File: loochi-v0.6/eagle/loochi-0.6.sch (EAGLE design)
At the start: 51 parts, among them IC1 ATTINY61M, J1 SPI_PRG, J2 POWER_JACKSMT3, P1 53047-0610, Q1 PMN25ENSOT457, Q2 PMN25ENSOT457, Q3 PMN25ENSOT457, U1 BLE112, U2 LZ4-00MC00BIGPADS, U3 LP2985

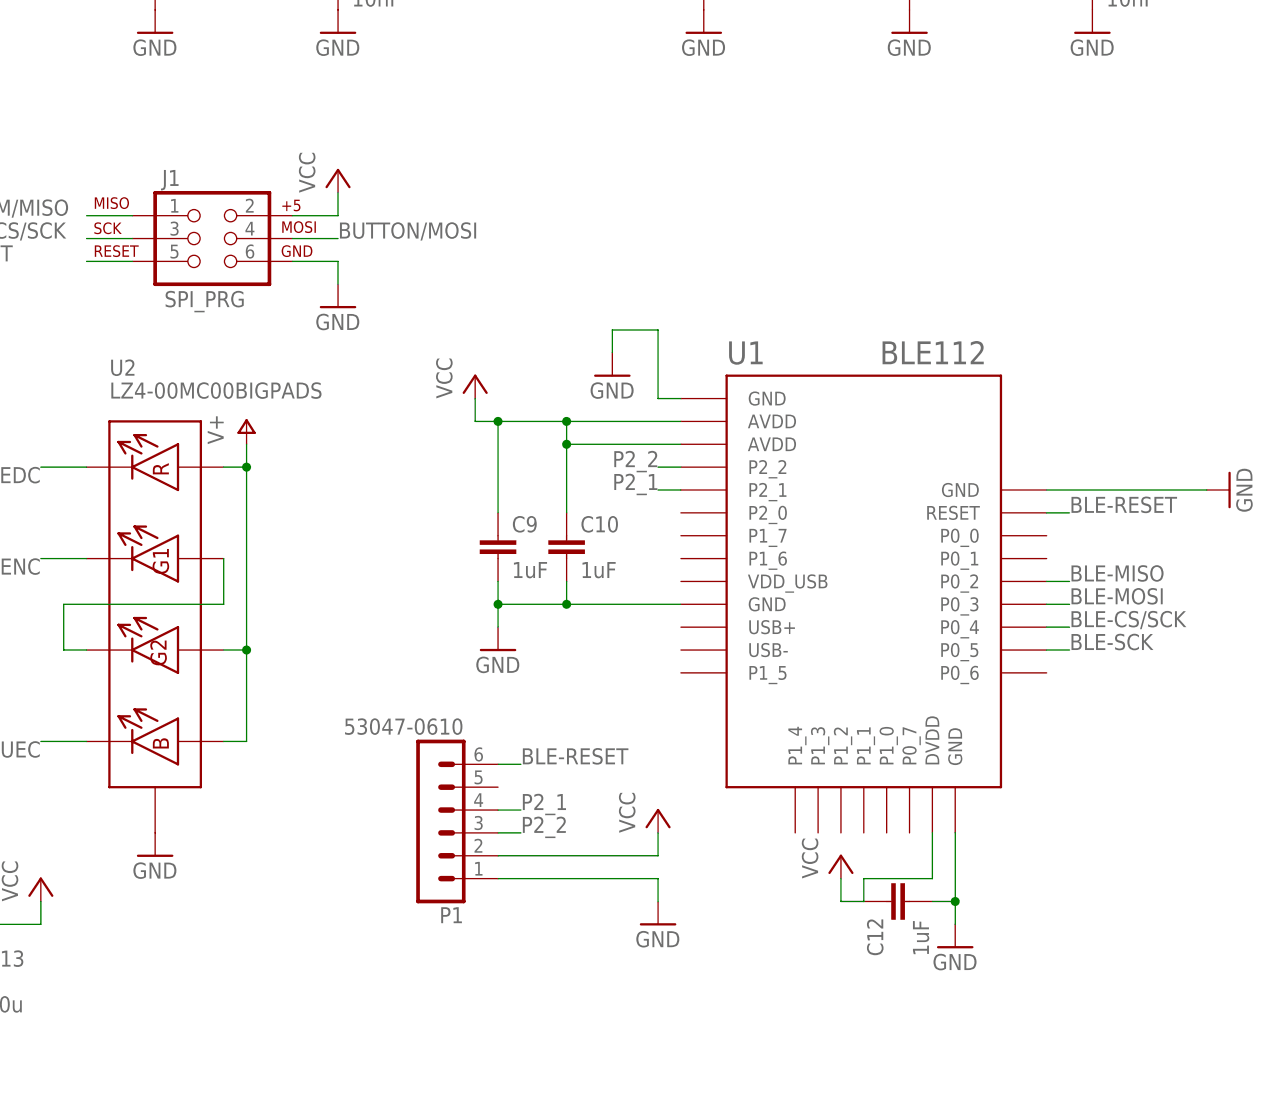
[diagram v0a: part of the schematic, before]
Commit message: Routed connections + Added SPI on BLE connector + Some cleaning/Rework
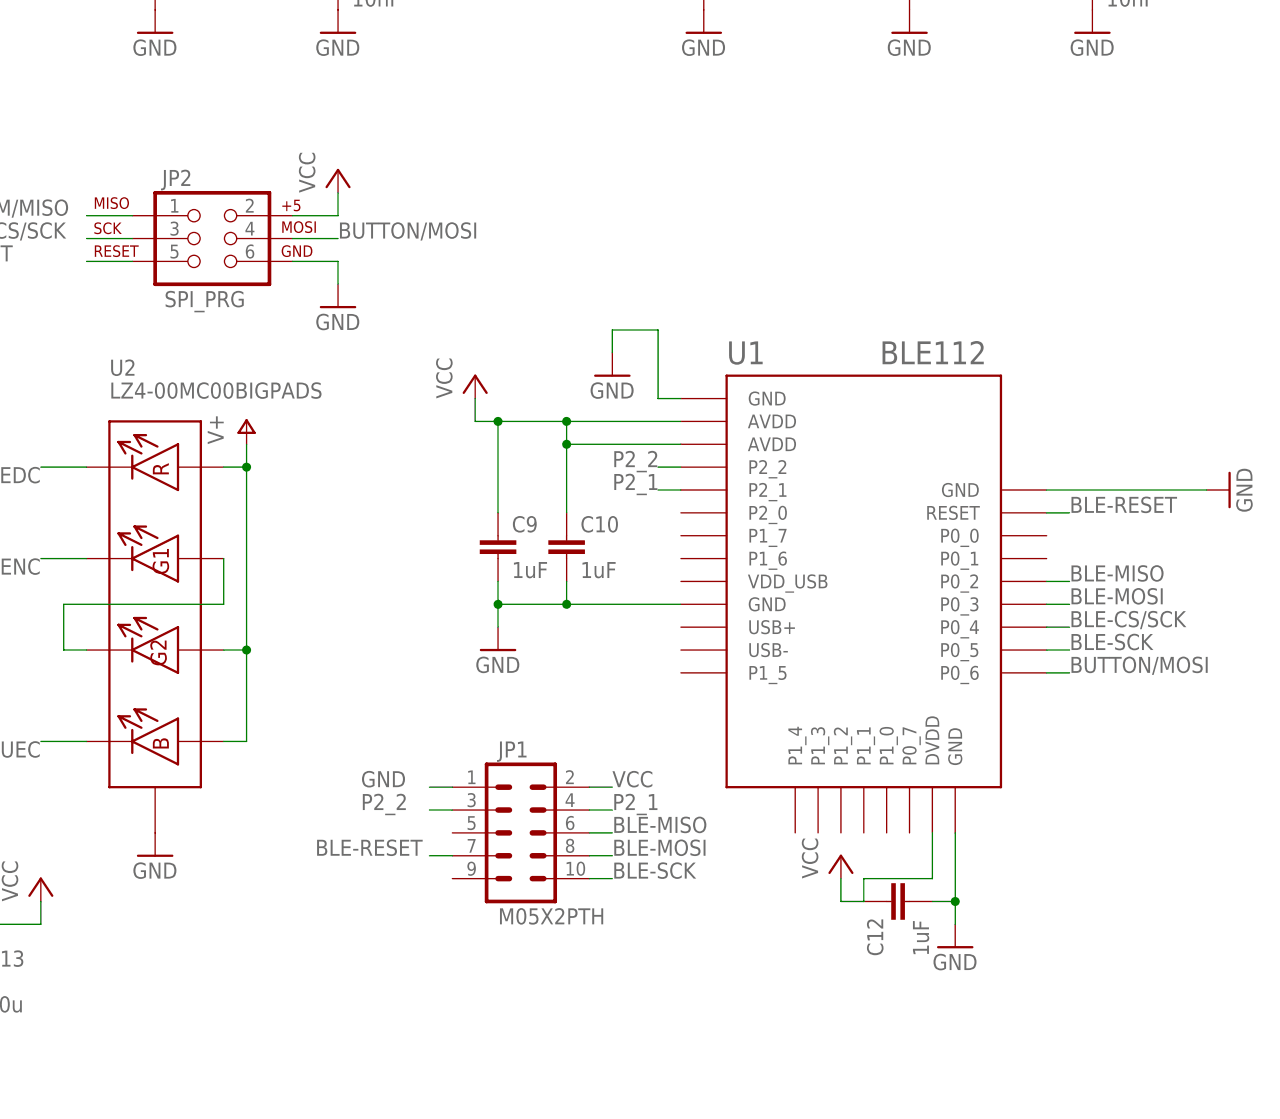
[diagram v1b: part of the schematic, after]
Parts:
- removed P1: 53047-0610, con-molex-picoblade:53047-0610
- added JP1: M05X2PTH, SparkFun:M05X2PTH
- renumbered J1 to JP2
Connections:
- net BLE-MISO: now also JP1.6
- net BLE-MOSI: now also JP1.8
- net BLE-RESET: now also JP1.7; no longer P1.6
- net BLE-SCK: now also JP1.10
- net BUTTON/MOSI: now also U1.P0_6
- net GND: now also JP1.1; no longer P1.1
- net P2_1: now also JP1.4; no longer P1.4
- net P2_2: now also JP1.3; no longer P1.3
- net VCC: now also JP1.2; no longer P1.2
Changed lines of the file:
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@@
 <parts>
 <part name="J2" library="power-connectors" deviceset="POWER_JACK" device="SMT3"/>
-<part name="J1" library="SparkFun" deviceset="AVR_SPI_PRG_6" device="NS" value="SPI_PRG"/>
+<part name="JP2" library="SparkFun" deviceset="AVR_SPI_PRG_6" device="NS" value="SPI_PRG"/>
 <part name="C7" library="rcl" deviceset="C-EU" device="C0603" value="0.1uF"/>
 <part name="C8" library="rcl" deviceset="C-EU" device="C0603" value="0.1uF"/>
@@
 <part name="C12" library="rcl" deviceset="C-EU" device="C0603" value="1uF"/>
 <part name="GND20" library="supply1" deviceset="GND" device=""/>
-<part name="P1" library="con-molex-picoblade" deviceset="53047-0610" device="">
-<attribute name="PARTNO" value="*"/>
-</part>
-<part name="P+10" library="supply1" deviceset="VCC" device=""/>
-<part name="GND21" library="supply1" deviceset="GND" device=""/>
 <part name="P+11" library="supply1" deviceset="VCC" device=""/>
 <part name="D4" library="diode-schottky" deviceset="DIODE-SCHOTTKY" device="D0603"/>
 <part name="D5" library="diode-schottky" deviceset="DIODE-SCHOTTKY" device="" value="PMEG4010CEH"/>
 <part name="S1" library="buttons" deviceset="TAC_SWITCH" device=""/>
+<part name="JP1" library="SparkFun" deviceset="M05X2" device="PTH"/>
 </parts>
 <sheets>
@@
 <instances>
 <instance part="J2" gate="G$1" x="15.24" y="20.32"/>
-<instance part="J1" gate="G$1" x="137.16" y="106.68"/>
+<instance part="JP2" gate="G$1" x="137.16" y="106.68"/>
 <instance part="C7" gate="G$1" x="12.7" y="101.6" smashed="yes" rot="R90">
 <attribute name="NAME" x="12.319" y="103.124" size="1.778" layer="95" rot="R90"/>
@@
 </instance>
 <instance part="GND20" gate="1" x="220.98" y="27.94"/>
-<instance part="P1" gate="G$1" x="165.1" y="43.18" rot="R180">
-<attribute name="PARTNO" x="165.1" y="43.18" size="1.778" layer="96" rot="R270" display="off"/>
-</instance>
-<instance part="P+10" gate="VCC" x="187.96" y="43.18"/>
-<instance part="GND21" gate="1" x="187.96" y="30.48"/>
 <instance part="P+11" gate="VCC" x="208.28" y="38.1"/>
 <instance part="D4" gate="G$1" x="93.98" y="40.64" rot="R180"/>
@@
 </instance>
 <instance part="S1" gate="S" x="40.64" y="53.34"/>
+<instance part="JP1" gate="G$1" x="172.72" y="40.64"/>
 </instances>
 <busses>
@@
 <net name="BUTTON/MOSI" class="0">
 <segment>
-<pinref part="J1" gate="G$1" pin="4"/>
+<pinref part="JP2" gate="G$1" pin="4"/>
 <wire x1="147.32" y1="106.68" x2="152.4" y2="106.68" width="0.1524" layer="91"/>
 <label x="152.4" y="106.68" size="1.778" layer="95"/>
@@
 <wire x1="45.72" y1="53.34" x2="50.8" y2="53.34" width="0.1524" layer="91"/>
 </segment>
+<segment>
+<pinref part="U1" gate="G$1" pin="P0_6"/>
+<wire x1="231.14" y1="58.42" x2="233.68" y2="58.42" width="0.1524" layer="91"/>
+<label x="233.68" y="58.42" size="1.778" layer="95"/>
+</segment>
 </net>
 <net name="RESET" class="0">
 <segment>
-<pinref part="J1" gate="G$1" pin="5"/>
+<pinref part="JP2" gate="G$1" pin="5"/>
 <wire x1="129.54" y1="104.14" x2="124.46" y2="104.14" width="0.1524" layer="91"/>
 <label x="109.22" y="104.14" size="1.778" layer="95"/>
@@
 <net name="BLE-CS/SCK" class="0">
 <segment>
-<pinref part="J1" gate="G$1" pin="3"/>
+<pinref part="JP2" gate="G$1" pin="3"/>
 <wire x1="129.54" y1="106.68" x2="124.46" y2="106.68" width="0.1524" layer="91"/>
 <label x="109.22" y="106.68" size="1.778" layer="95"/>
@@
 </segment>
 <segment>
-<pinref part="J1" gate="G$1" pin="6"/>
+<pinref part="JP2" gate="G$1" pin="6"/>
 <wire x1="147.32" y1="104.14" x2="152.4" y2="104.14" width="0.1524" layer="91"/>
 <wire x1="152.4" y1="104.14" x2="152.4" y2="101.6" width="0.1524" layer="91"/>
@@
 </segment>
 <segment>
-<pinref part="P1" gate="G$1" pin="1"/>
-<wire x1="170.18" y1="35.56" x2="187.96" y2="35.56" width="0.1524" layer="91"/>
-<wire x1="187.96" y1="35.56" x2="187.96" y2="33.02" width="0.1524" layer="91"/>
-<pinref part="GND21" gate="1" pin="GND"/>
+<pinref part="JP1" gate="G$1" pin="1"/>
+<wire x1="165.1" y1="45.72" x2="162.56" y2="45.72" width="0.1524" layer="91"/>
+<label x="154.94" y="45.72" size="1.778" layer="95"/>
 </segment>
 </net>
@@
 </segment>
 <segment>
-<pinref part="J1" gate="G$1" pin="2"/>
+<pinref part="JP2" gate="G$1" pin="2"/>
 <wire x1="147.32" y1="109.22" x2="152.4" y2="109.22" width="0.1524" layer="91"/>
 <wire x1="152.4" y1="109.22" x2="152.4" y2="111.76" width="0.1524" layer="91"/>
@@
 </segment>
 <segment>
-<pinref part="P1" gate="G$1" pin="2"/>
-<wire x1="170.18" y1="38.1" x2="187.96" y2="38.1" width="0.1524" layer="91"/>
-<wire x1="187.96" y1="38.1" x2="187.96" y2="40.64" width="0.1524" layer="91"/>
-<pinref part="P+10" gate="VCC" pin="VCC"/>
-</segment>
-<segment>
 <pinref part="P+11" gate="VCC" pin="VCC"/>
 <wire x1="208.28" y1="35.56" x2="208.28" y2="33.02" width="0.1524" layer="91"/>
@@
 <wire x1="218.44" y1="35.56" x2="218.44" y2="40.64" width="0.1524" layer="91"/>
 </segment>
+<segment>
+<pinref part="JP1" gate="G$1" pin="2"/>
+<wire x1="180.34" y1="45.72" x2="182.88" y2="45.72" width="0.1524" layer="91"/>
+<label x="182.88" y="45.72" size="1.778" layer="95"/>
+</segment>
 </net>
 <net name="N$7" class="0">
@@
 <label x="233.68" y="66.04" size="1.778" layer="95"/>
 </segment>
+<segment>
+<pinref part="JP1" gate="G$1" pin="8"/>
+<wire x1="180.34" y1="38.1" x2="182.88" y2="38.1" width="0.1524" layer="91"/>
+<label x="182.88" y="38.1" size="1.778" layer="95"/>
+</segment>
 </net>
 <net name="BLE-SCK" class="0">
@@
 <label x="233.68" y="60.96" size="1.778" layer="95"/>
 </segment>
+<segment>
+<pinref part="JP1" gate="G$1" pin="10"/>
+<wire x1="180.34" y1="35.56" x2="182.88" y2="35.56" width="0.1524" layer="91"/>
+<label x="182.88" y="35.56" size="1.778" layer="95"/>
+</segment>
 </net>
 <net name="BLE-MISO" class="0">
@@
 <label x="233.68" y="68.58" size="1.778" layer="95"/>
 </segment>
+<segment>
+<pinref part="JP1" gate="G$1" pin="6"/>
+<wire x1="180.34" y1="40.64" x2="182.88" y2="40.64" width="0.1524" layer="91"/>
+<label x="182.88" y="40.64" size="1.778" layer="95"/>
+</segment>
 </net>
 <net name="N$13" class="0">
@@
 </segment>
 <segment>
-<pinref part="J1" gate="G$1" pin="1"/>
+<pinref part="JP2" gate="G$1" pin="1"/>
 <wire x1="129.54" y1="109.22" x2="124.46" y2="109.22" width="0.1524" layer="91"/>
 <label x="109.22" y="109.22" size="1.778" layer="95"/>
@@
 </segment>
 <segment>
-<pinref part="P1" gate="G$1" pin="3"/>
-<wire x1="170.18" y1="40.64" x2="172.72" y2="40.64" width="0.1524" layer="91"/>
-<label x="172.72" y="40.64" size="1.778" layer="95"/>
+<pinref part="JP1" gate="G$1" pin="3"/>
+<wire x1="165.1" y1="43.18" x2="162.56" y2="43.18" width="0.1524" layer="91"/>
+<label x="154.94" y="43.18" size="1.778" layer="95"/>
 </segment>
 </net>
@@
 </segment>
 <segment>
-<pinref part="P1" gate="G$1" pin="4"/>
-<wire x1="170.18" y1="43.18" x2="172.72" y2="43.18" width="0.1524" layer="91"/>
-<label x="172.72" y="43.18" size="1.778" layer="95"/>
+<pinref part="JP1" gate="G$1" pin="4"/>
+<wire x1="180.34" y1="43.18" x2="182.88" y2="43.18" width="0.1524" layer="91"/>
+<label x="182.88" y="43.18" size="1.778" layer="95"/>
 </segment>
 </net>
 <net name="BLE-RESET" class="0">
-<segment>
-<pinref part="P1" gate="G$1" pin="6"/>
-<wire x1="170.18" y1="48.26" x2="172.72" y2="48.26" width="0.1524" layer="91"/>
-<label x="172.72" y="48.26" size="1.778" layer="95"/>
-</segment>
 <segment>
 <pinref part="U1" gate="G$1" pin="RESET"/>
@@
 <label x="233.68" y="76.2" size="1.778" layer="95"/>
 </segment>
-</net>
+<segment>
+<pinref part="JP1" gate="G$1" pin="7"/>
+<wire x1="165.1" y1="38.1" x2="162.56" y2="38.1" width="0.1524" layer="91"/>
+<label x="149.86" y="38.1" size="1.778" layer="95"/>
+</segment>
+</net>
